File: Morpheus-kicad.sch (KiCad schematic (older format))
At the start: 58 parts, among them J1 Conn_02x03_Odd_Even, J2 Conn_02x03_Odd_Even, J3 Conn_02x03_Odd_Even, J4 Conn_02x03_Odd_Even, J5 Conn_02x05_Counter_Clockwise, Q1 IRLZ44N, Q2 IRLB3034PBF, Q3 IRLZ44N, U1 Pololu Driver, U2 Pololu Driver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

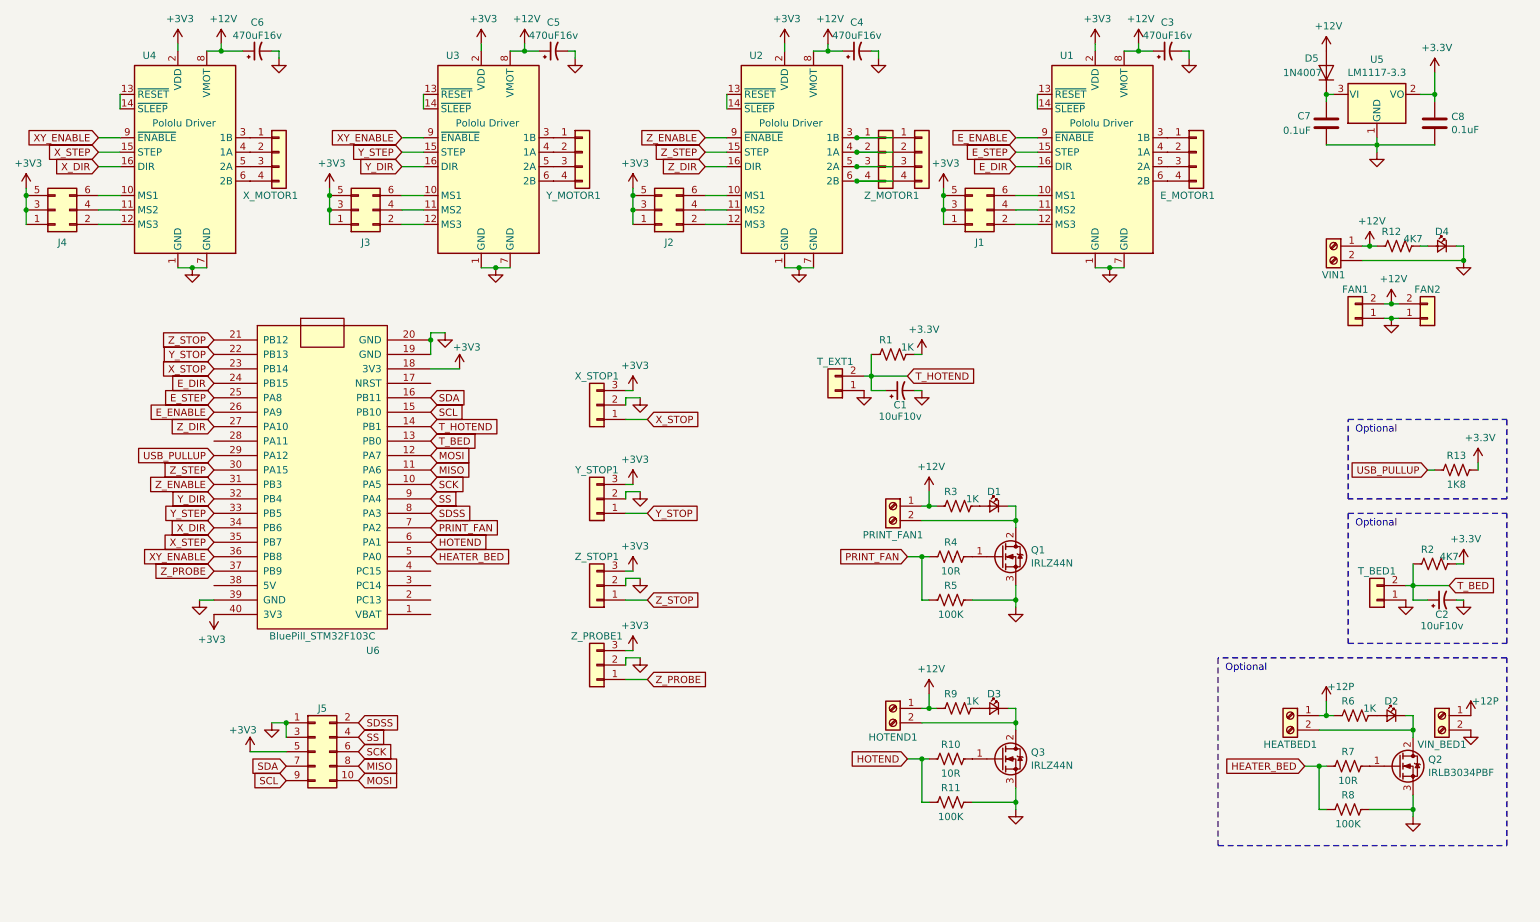
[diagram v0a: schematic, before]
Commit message: Add reverse current protection
Added a 1N4007 or similar diode to protect from reverse current. Bear in mind that, without a fuse, it will just burn and let current pass again, damaging components.
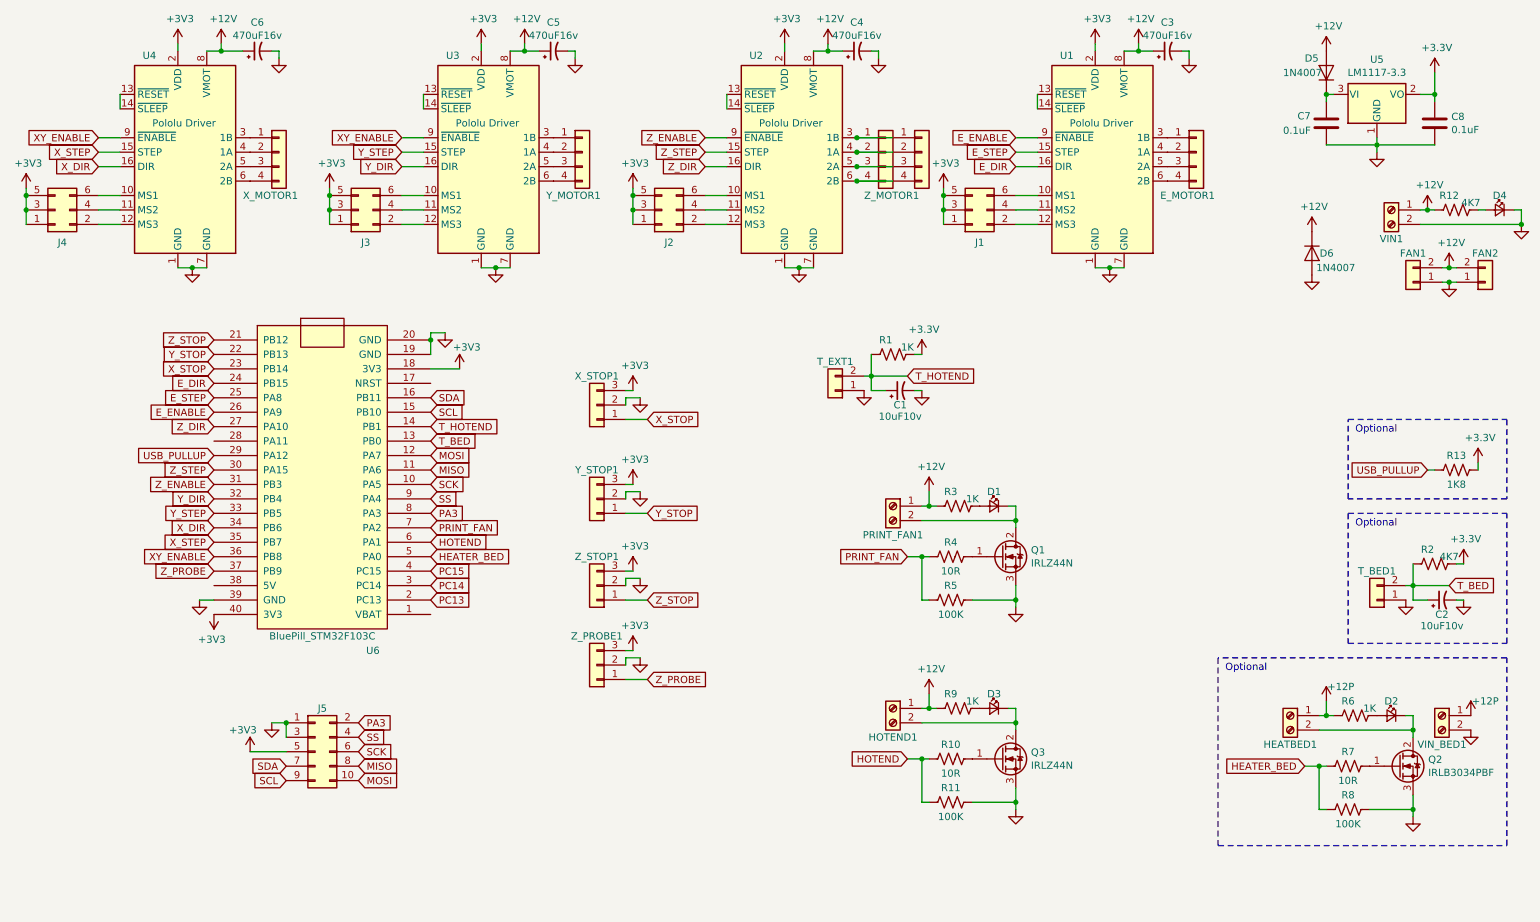
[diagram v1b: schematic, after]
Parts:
- added D6: 1N4007, Diode_THT:D_DO-35_SOD27_P2.54mm_Vertical_AnodeUp, symbol Diode:1N4007
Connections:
- net +12V: now also D6.1 (K)
- net GND: now also D6.2 (A)
- net PC13: now reaches U6.2 (PC13)
- net PC14: now reaches U6.3 (PC14)
- net PC15: now reaches U6.4 (PC15)
- net SDSS renamed PA3
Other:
- moved on the sheet: D4, FAN1, FAN2, R12, VIN1
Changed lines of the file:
@@
 Title "MORPHEUS Board by SPON!"
 Date ""
-Rev "0.4"
+Rev "0.5"
 Comp "Released under GPLv3"
 Comment1 ""
@@
 SS
 Text GLabel 3400 4000 2    50   Input ~ 0
-SDSS
+PA3
 Text GLabel 3400 4100 2    50   Input ~ 0
 PRINT_FAN
@@
 SCL
 Text GLabel 2900 5450 2    50   Input ~ 0
-SDSS
+PA3
 Text GLabel 2900 5550 2    50   Input ~ 0
 SS
@@
 L Connector:Screw_Terminal_01x02 VIN1
 U 1 1 5BEB6D61
-P 9650 2150
-F 0 "VIN1" H 9650 1950 50  0000 C CNN
-F 1 "VIN" H 9730 2051 50  0001 L CNN
-F 2 "TerminalBlock_Phoenix:TerminalBlock_Phoenix_MKDS-1,5-2_1x02_P5.00mm_Horizontal" H 9650 2150 50  0001 C CNN
-F 3 "~" H 9650 2150 50  0001 C CNN
-	1    9650 2150
+P 10050 1900
+F 0 "VIN1" H 10050 1700 50  0000 C CNN
+F 1 "VIN" H 10130 1801 50  0001 L CNN
+F 2 "TerminalBlock_Phoenix:TerminalBlock_Phoenix_MKDS-1,5-2_1x02_P5.00mm_Horizontal" H 10050 1900 50  0001 C CNN
+F 3 "~" H 10050 1900 50  0001 C CNN
+	1    10050 1900
 	-1   0    0    -1
 $EndComp
@@
 L power:+12V #PWR0130
 U 1 1 5BECA804
-P 9900 2150
-F 0 "#PWR0130" H 9900 2000 50  0001 C CNN
-F 1 "+12V" H 9915 2323 50  0000 C CNN
-F 2 "" H 9900 2150 50  0001 C CNN
-F 3 "" H 9900 2150 50  0001 C CNN
-	1    9900 2150
+P 10300 1900
+F 0 "#PWR0130" H 10300 1750 50  0001 C CNN
+F 1 "+12V" H 10315 2073 50  0000 C CNN
+F 2 "" H 10300 1900 50  0001 C CNN
+F 3 "" H 10300 1900 50  0001 C CNN
+	1    10300 1900
 	1    0    0    -1
 $EndComp
@@
 L Device:R_US R12
 U 1 1 5BECCF64
-P 10100 2150
-F 0 "R12" V 10000 2100 50  0000 C CNN
-F 1 "4K7" V 10050 2250 50  0000 C CNN
-F 2 "Resistor_THT:R_Axial_DIN0207_L6.3mm_D2.5mm_P7.62mm_Horizontal" V 10140 2140 50  0001 C CNN
-F 3 "~" H 10100 2150 50  0001 C CNN
-	1    10100 2150
+P 10500 1900
+F 0 "R12" V 10400 1850 50  0000 C CNN
+F 1 "4K7" V 10450 2000 50  0000 C CNN
+F 2 "Resistor_THT:R_Axial_DIN0207_L6.3mm_D2.5mm_P7.62mm_Horizontal" V 10540 1890 50  0001 C CNN
+F 3 "~" H 10500 1900 50  0001 C CNN
+	1    10500 1900
 	0    1    1    0
 $EndComp
@@
 L Device:LED_Small D4
 U 1 1 5BECD15E
-P 10400 2150
-F 0 "D4" H 10400 2250 50  0000 C CNN
-F 1 "LED_Small" H 10400 2036 50  0001 C CNN
-F 2 "LED_THT:LED_D3.0mm_Clear" V 10400 2150 50  0001 C CNN
-F 3 "~" V 10400 2150 50  0001 C CNN
-	1    10400 2150
+P 10800 1900
+F 0 "D4" H 10800 2000 50  0000 C CNN
+F 1 "LED_Small" H 10800 1786 50  0001 C CNN
+F 2 "LED_THT:LED_D3.0mm_Clear" V 10800 1900 50  0001 C CNN
+F 3 "~" V 10800 1900 50  0001 C CNN
+	1    10800 1900
 	-1   0    0    -1
 $EndComp
@@
 L power:GND #PWR0131
 U 1 1 5BECD2C8
-P 10550 2250
-F 0 "#PWR0131" H 10550 2000 50  0001 C CNN
-F 1 "GND" H 10555 2077 50  0001 C CNN
-F 2 "" H 10550 2250 50  0001 C CNN
-F 3 "" H 10550 2250 50  0001 C CNN
-	1    10550 2250
-	1    0    0    -1
-$EndComp
-Wire Wire Line
-	9850 2150 9900 2150
-Connection ~ 9900 2150
-Wire Wire Line
-	9900 2150 9950 2150
-Wire Wire Line
-	10250 2150 10300 2150
-Wire Wire Line
-	10500 2150 10550 2150
-Wire Wire Line
-	10550 2150 10550 2250
-Wire Wire Line
-	9850 2250 10550 2250
-Connection ~ 10550 2250
+P 10950 2000
+F 0 "#PWR0131" H 10950 1750 50  0001 C CNN
+F 1 "GND" H 10955 1827 50  0001 C CNN
+F 2 "" H 10950 2000 50  0001 C CNN
+F 3 "" H 10950 2000 50  0001 C CNN
+	1    10950 2000
+	1    0    0    -1
+$EndComp
+Wire Wire Line
+	10250 1900 10300 1900
+Connection ~ 10300 1900
+Wire Wire Line
+	10300 1900 10350 1900
+Wire Wire Line
+	10650 1900 10700 1900
+Wire Wire Line
+	10900 1900 10950 1900
+Wire Wire Line
+	10950 1900 10950 2000
+Wire Wire Line
+	10250 2000 10950 2000
+Connection ~ 10950 2000
 $Comp
 L power:+12P #PWR0132
@@
 L Connector_Generic:Conn_01x02 FAN1
 U 1 1 5BEEF3EB
-P 9800 2650
-F 0 "FAN1" H 9800 2450 50  0000 C CNN
-F 1 "Conn_01x02" H 9720 2416 50  0001 C CNN
-F 2 "Connector_PinHeader_2.54mm:PinHeader_1x02_P2.54mm_Vertical" H 9800 2650 50  0001 C CNN
-F 3 "~" H 9800 2650 50  0001 C CNN
-	1    9800 2650
+P 10200 2400
+F 0 "FAN1" H 10200 2200 50  0000 C CNN
+F 1 "Conn_01x02" H 10120 2166 50  0001 C CNN
+F 2 "Connector_PinHeader_2.54mm:PinHeader_1x02_P2.54mm_Vertical" H 10200 2400 50  0001 C CNN
+F 3 "~" H 10200 2400 50  0001 C CNN
+	1    10200 2400
 	-1   0    0    1
 $EndComp
@@
 L Connector_Generic:Conn_01x02 FAN2
 U 1 1 5BEF45CE
-P 10300 2650
-F 0 "FAN2" H 10300 2450 50  0000 C CNN
-F 1 "Conn_01x02" H 10220 2416 50  0001 C CNN
-F 2 "Connector_PinHeader_2.54mm:PinHeader_1x02_P2.54mm_Vertical" H 10300 2650 50  0001 C CNN
-F 3 "~" H 10300 2650 50  0001 C CNN
-	1    10300 2650
+P 10700 2400
+F 0 "FAN2" H 10700 2200 50  0000 C CNN
+F 1 "Conn_01x02" H 10620 2166 50  0001 C CNN
+F 2 "Connector_PinHeader_2.54mm:PinHeader_1x02_P2.54mm_Vertical" H 10700 2400 50  0001 C CNN
+F 3 "~" H 10700 2400 50  0001 C CNN
+	1    10700 2400
 	1    0    0    1
 $EndComp
@@
 L power:+12V #PWR0134
 U 1 1 5BEF93AF
-P 10050 2550
-F 0 "#PWR0134" H 10050 2400 50  0001 C CNN
-F 1 "+12V" H 10065 2723 50  0000 C CNN
-F 2 "" H 10050 2550 50  0001 C CNN
-F 3 "" H 10050 2550 50  0001 C CNN
-	1    10050 2550
+P 10450 2300
+F 0 "#PWR0134" H 10450 2150 50  0001 C CNN
+F 1 "+12V" H 10465 2473 50  0000 C CNN
+F 2 "" H 10450 2300 50  0001 C CNN
+F 3 "" H 10450 2300 50  0001 C CNN
+	1    10450 2300
 	1    0    0    -1
 $EndComp
@@
 L power:GND #PWR0135
 U 1 1 5BEFBA7E
-P 10050 2650
-F 0 "#PWR0135" H 10050 2400 50  0001 C CNN
-F 1 "GND" H 10055 2477 50  0001 C CNN
-F 2 "" H 10050 2650 50  0001 C CNN
-F 3 "" H 10050 2650 50  0001 C CNN
-	1    10050 2650
-	1    0    0    -1
-$EndComp
-Wire Wire Line
-	10000 2550 10050 2550
-Connection ~ 10050 2550
-Wire Wire Line
-	10050 2550 10100 2550
-Wire Wire Line
-	10100 2650 10050 2650
-Connection ~ 10050 2650
-Wire Wire Line
-	10050 2650 10000 2650
+P 10450 2400
+F 0 "#PWR0135" H 10450 2150 50  0001 C CNN
+F 1 "GND" H 10455 2227 50  0001 C CNN
+F 2 "" H 10450 2400 50  0001 C CNN
+F 3 "" H 10450 2400 50  0001 C CNN
+	1    10450 2400
+	1    0    0    -1
+$EndComp
+Wire Wire Line
+	10400 2300 10450 2300
+Connection ~ 10450 2300
+Wire Wire Line
+	10450 2300 10500 2300
+Wire Wire Line
+	10500 2400 10450 2400
+Connection ~ 10450 2400
+Wire Wire Line
+	10450 2400 10400 2400
 $Comp
 L power:GND #PWR0136
@@
 	3400 2800 3400 2900
 Connection ~ 3400 2800
+$Comp
+L Diode:1N4007 D6
+U 1 1 5D517BE9
+P 9500 2200
+F 0 "D6" V 9500 2350 50  0000 R CNN
+F 1 "1N4007" V 9600 2500 50  0000 R CNN
+F 2 "Diode_THT:D_DO-35_SOD27_P2.54mm_Vertical_AnodeUp" H 9500 2025 50  0001 C CNN
+F 3 "http://www.vishay.com/docs/88503/1n4001.pdf" H 9500 2200 50  0001 C CNN
+	1    9500 2200
+	0    1    1    0
+$EndComp
+$Comp
+L power:+12V #PWR0157
+U 1 1 5D53090A
+P 9500 2050
+F 0 "#PWR0157" H 9500 1900 50  0001 C CNN
+F 1 "+12V" H 9515 2223 50  0000 C CNN
+F 2 "" H 9500 2050 50  0001 C CNN
+F 3 "" H 9500 2050 50  0001 C CNN
+	1    9500 2050
+	1    0    0    -1
+$EndComp
+$Comp
+L power:GND #PWR0158
+U 1 1 5D538D45
+P 9500 2350
+F 0 "#PWR0158" H 9500 2100 50  0001 C CNN
+F 1 "GND" H 9505 2177 50  0001 C CNN
+F 2 "" H 9500 2350 50  0001 C CNN
+F 3 "" H 9500 2350 50  0001 C CNN
+	1    9500 2350
+	1    0    0    -1
+$EndComp
+Text GLabel 3400 4400 2    50   Input ~ 0
+PC15
+Text GLabel 3400 4500 2    50   Input ~ 0
+PC14
+Text GLabel 3400 4600 2    50   Input ~ 0
+PC13
 $EndSCHEMATC

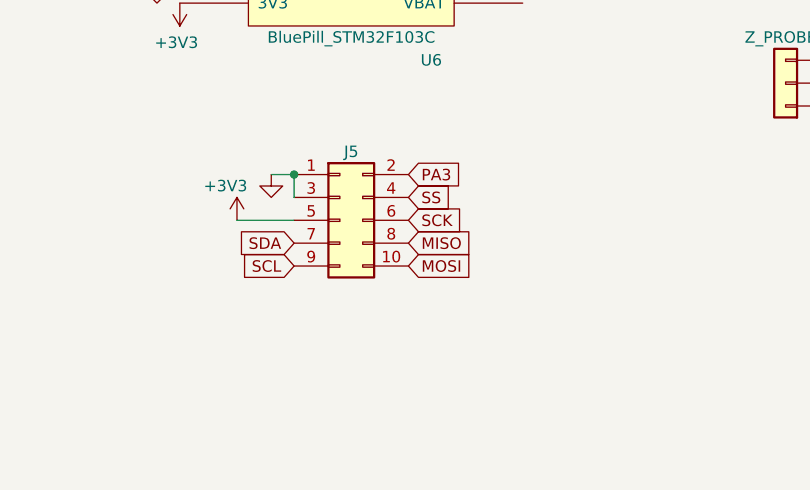
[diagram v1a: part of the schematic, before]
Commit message: Add header
Added a header for the unused pins, just to make them usable.
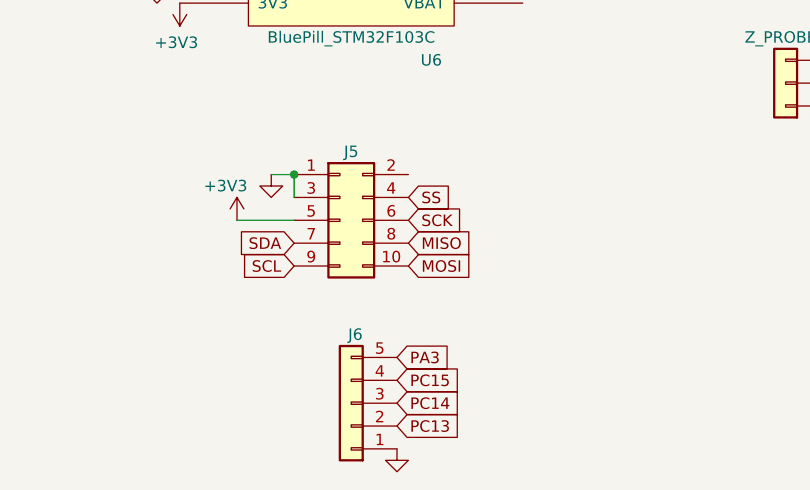
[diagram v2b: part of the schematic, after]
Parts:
- added J6: Conn_01x05, Connector_PinHeader_2.54mm:PinHeader_1x05_P2.54mm_Vertical, symbol Connector_Generic:Conn_01x05
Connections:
- net GND: now also J6.1 (Pin_1)
- net PA3: now also J6.5 (Pin_5); no longer J5.2 (Pin_2)
- net PC13: now also J6.2 (Pin_2)
- net PC14: now also J6.3 (Pin_3)
- net PC15: now also J6.4 (Pin_4)
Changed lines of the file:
@@
 EESchema Schematic File Version 4
 LIBS:Morpheus-kicad-cache
-EELAYER 26 0
+EELAYER 30 0
 EELAYER END
 $Descr A4 11693 8268
@@
 Title "MORPHEUS Board by SPON!"
 Date ""
-Rev "0.5"
+Rev "0.6"
 Comp "Released under GPLv3"
 Comment1 ""
@@
 Text GLabel 2400 5850 0    50   Input ~ 0
 SCL
-Text GLabel 2900 5450 2    50   Input ~ 0
+Text GLabel 2850 6250 2    50   Input ~ 0
 PA3
 Text GLabel 2900 5550 2    50   Input ~ 0
@@
 	1    0    0    -1
 $EndComp
+$Comp
+L Connector_Generic:Conn_01x05 J6
+U 1 1 5DD7FDA2
+P 2650 6450
+F 0 "J6" H 2600 6150 50  0000 L CNN
+F 1 "Conn_01x05" H 2730 6399 50  0001 L CNN
+F 2 "Connector_PinHeader_2.54mm:PinHeader_1x05_P2.54mm_Vertical" H 2650 6450 50  0001 C CNN
+F 3 "~" H 2650 6450 50  0001 C CNN
+	1    2650 6450
+	-1   0    0    1
+$EndComp
 Text GLabel 3400 4400 2    50   Input ~ 0
 PC15
@@
 Text GLabel 3400 4600 2    50   Input ~ 0
 PC13
+Text GLabel 2850 6350 2    50   Input ~ 0
+PC15
+Text GLabel 2850 6450 2    50   Input ~ 0
+PC14
+Text GLabel 2850 6550 2    50   Input ~ 0
+PC13
+$Comp
+L power:GND #PWR0159
+U 1 1 5DDBE61A
+P 2850 6650
+F 0 "#PWR0159" H 2850 6400 50  0001 C CNN
+F 1 "GND" H 2855 6477 50  0001 C CNN
+F 2 "" H 2850 6650 50  0001 C CNN
+F 3 "" H 2850 6650 50  0001 C CNN
+	1    2850 6650
+	1    0    0    -1
+$EndComp
 $EndSCHEMATC
